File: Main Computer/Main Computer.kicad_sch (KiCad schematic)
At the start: 6 parts, among them J1 Pi 5 GPIO HEADER, J2 Conn_01x06, J3 Conn_01x02, J4 CAN to outer connector, U2 E01-ML01DP5

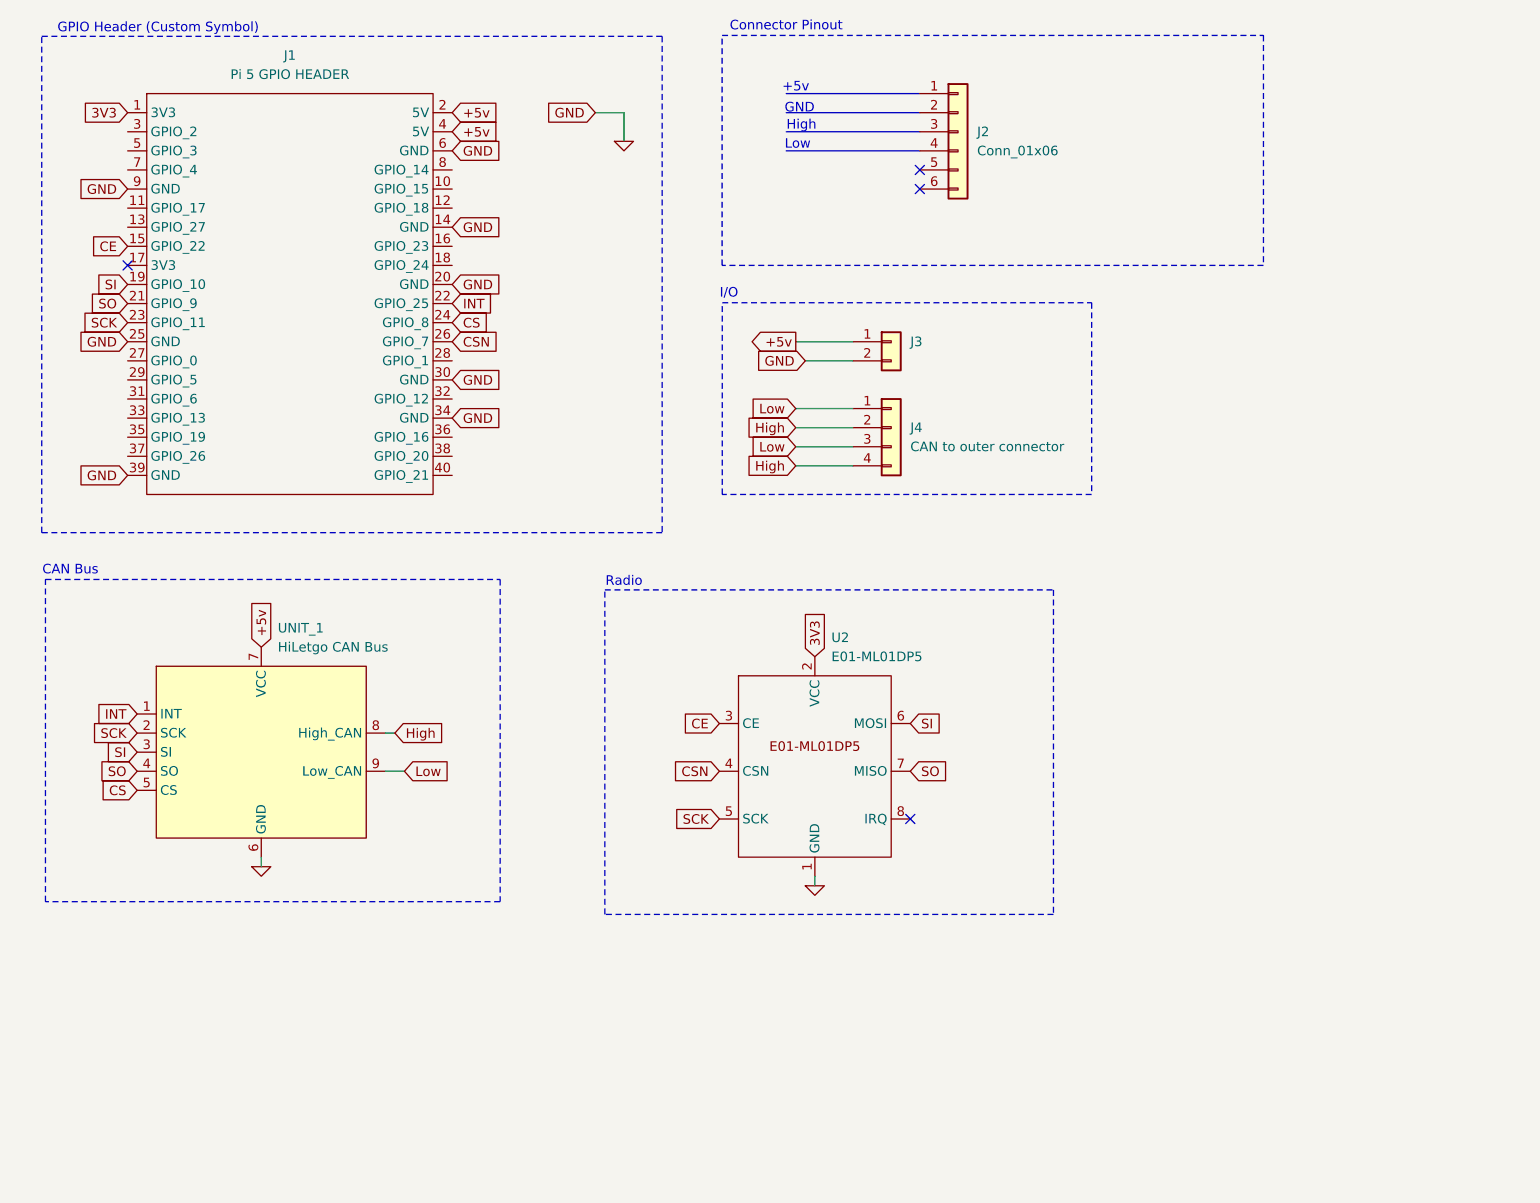
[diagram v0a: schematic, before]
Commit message: need to align pinheader
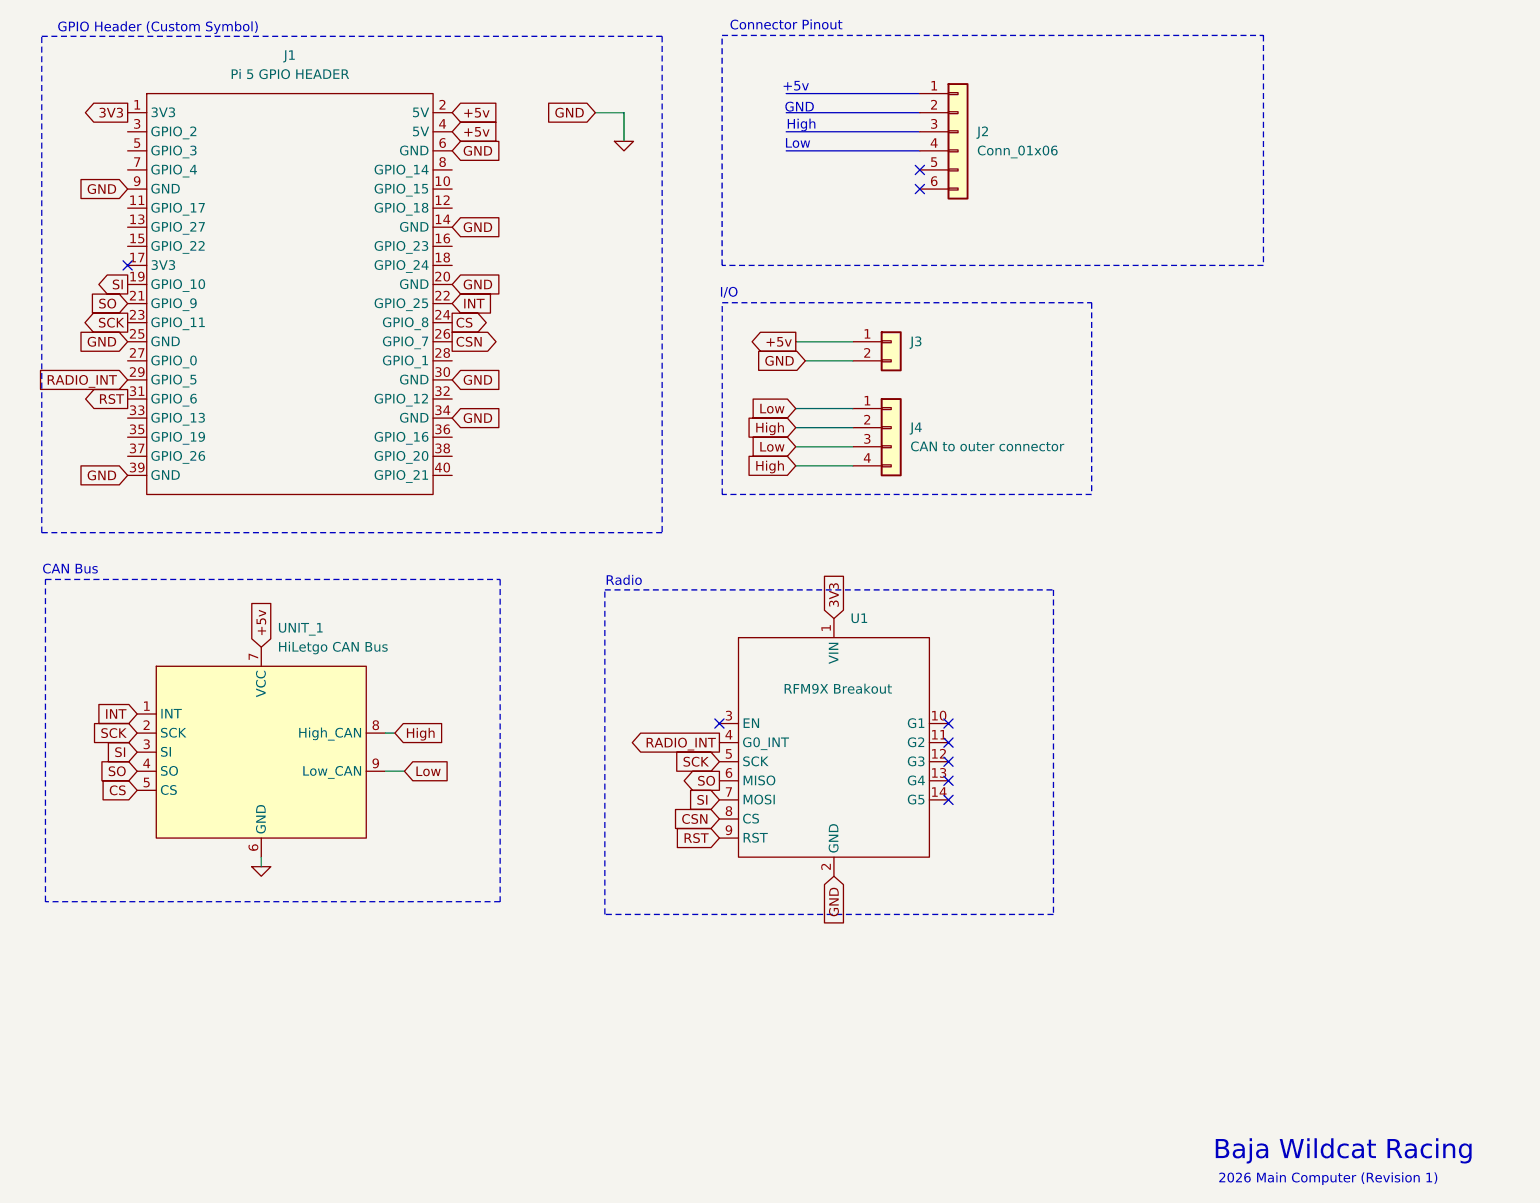
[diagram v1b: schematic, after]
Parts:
- removed U2: E01-ML01DP5, 0_custom:Ebyte E01-ML01DP5, symbol 0_custom:Ebyte_E01-ML01DP5
- added U1: RFM9X Breakout, Baja SAE Footprints:Adafruit RFM95W Breakout, symbol Baja SAE Symbols:Adafruit_RFM95W_Breakout
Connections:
- net 0: now also U1.2 (GND)
- net 3V3: now also U1.1 (VIN)
- net CSN: now also U1.8 (CS)
- net SCK: now also U1.5 (SCK)
- net SI: now also U1.7 (MOSI)
- net SO: now also U1.6 (MISO)
- net RADIO_INT: now reaches J1.29 (GPIO_5)
- net RADIO_INT: now also U1.4 (G0_INT)
- net RST: now reaches J1.31 (GPIO_6)
- net RST: now also U1.9 (RST)
- net CE: no longer names the net of J1.15 (GPIO_22)
- no-connect marks 4 -> 9
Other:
- note added: "2026 Main Computer (Revision 1)"
- note added: "Baja Wildcat Racing"

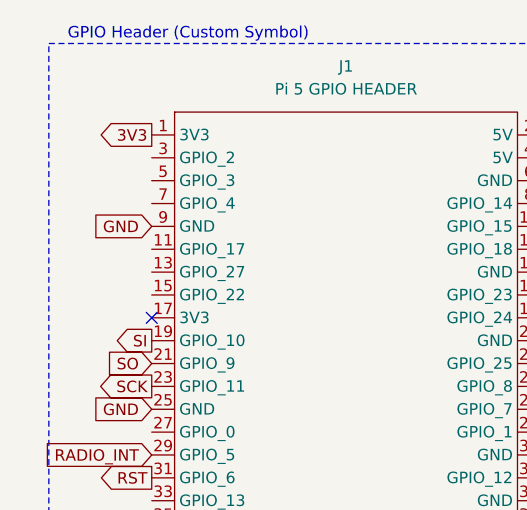
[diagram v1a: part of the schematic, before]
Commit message: routing done
still need to make can attachment holes bigger
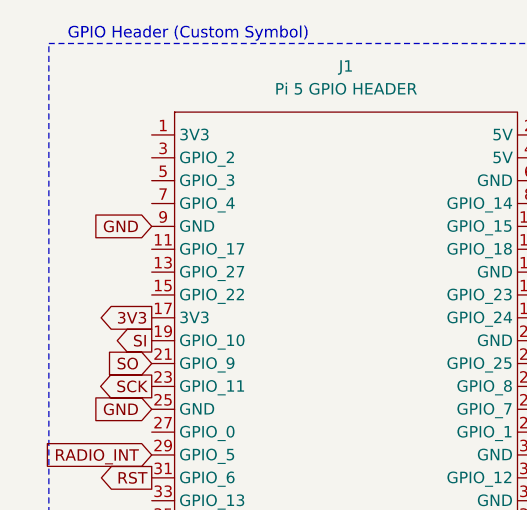
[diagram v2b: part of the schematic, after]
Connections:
- net 3V3: now also J1.17 (3V3); no longer J1.1 (3V3)
- no-connect marks 9 -> 8
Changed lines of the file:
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@@
 	)
 	(no_connect
-		(at 36.83 52.07)
-	)
-	(no_connect
 		(at 115.57 113.03)
 	)
@@
 	(global_label "3V3"
 		(shape output)
-		(at 36.83 31.75 180)
+		(at 36.83 52.07 180)
 		(fields_autoplaced yes)
 		(effects
@@
 		)
 		(property "Intersheetrefs" "${INTERSHEET_REFS}"
-			(at 30.3372 31.75 0)
+			(at 30.3372 52.07 0)
 			(effects
 				(font

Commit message: workprogress
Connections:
- net SCK: no longer UNIT_1.2 (SCK)
- net SI: no longer UNIT_1.3 (SI)
- net SO: no longer UNIT_1.4 (SO)
- net CAN_INT: now reaches J1.15 (GPIO_22)
- net CAN_INT: now also UNIT_1.1 (INT)
- net SPI1_MISO: now reaches J1.35 (GPIO_19)
- net SPI1_MISO: now also UNIT_1.4 (SO)
- net CAN_CS: now reaches J1.36 (GPIO_16)
- net CAN_CS: now also UNIT_1.5 (CS)
- net SPI1_MOSI: now reaches J1.38 (GPIO_20)
- net SPI1_MOSI: now also UNIT_1.3 (SI)
- net SPI1_SCK: now reaches J1.40 (GPIO_21)
- net SPI1_SCK: now also UNIT_1.2 (SCK)
- net CS: no longer names the net of J1.24 (GPIO_8)
- net CS: no longer UNIT_1.5 (CS)
- net INT: no longer names the net of J1.22 (GPIO_25)
- net INT: no longer UNIT_1.1 (INT)
- no-connect marks 8 -> 26

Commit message: PCB KNOWN GOOD
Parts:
- J3: footprint Connector_Wire:SolderWire-0.75sqmm_1x02_P4.8mm_D1.25mm_OD2.3mm -> Connector_Wire:SolderWire-1.5sqmm_1x02_P7.8mm_D1.7mm_OD3.9mm
- J4: footprint Connector_Wire:SolderWire-0.1sqmm_1x04_P3.6mm_D0.4mm_OD1mm -> Connector_Wire:SolderWire-0.5sqmm_1x04_P4.6mm_D0.9mm_OD2.1mm
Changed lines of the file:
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@@
 			)
 		)
-		(property "Footprint" "Connector_Wire:SolderWire-0.75sqmm_1x02_P4.8mm_D1.25mm_OD2.3mm"
+		(property "Footprint" "Connector_Wire:SolderWire-1.5sqmm_1x02_P7.8mm_D1.7mm_OD3.9mm"
 			(at 138.43 62.23 0)
 			(effects
@@
 			)
 		)
-		(property "Footprint" "Connector_Wire:SolderWire-0.1sqmm_1x04_P3.6mm_D0.4mm_OD1mm"
+		(property "Footprint" "Connector_Wire:SolderWire-0.5sqmm_1x04_P4.6mm_D0.9mm_OD2.1mm"
 			(at 138.43 73.66 0)
 			(effects
